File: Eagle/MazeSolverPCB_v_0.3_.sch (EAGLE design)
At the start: 26 parts, among them X1 TSW-113-02-S-S, X2 TSW-116-02-S-S, X3 TSW-113-02-S-S, X4 TSW-103-02-S-S, X5 TSW-103-02-S-S, X6 TSW-103-02-S-S, X7 TSW-103-02-S-S

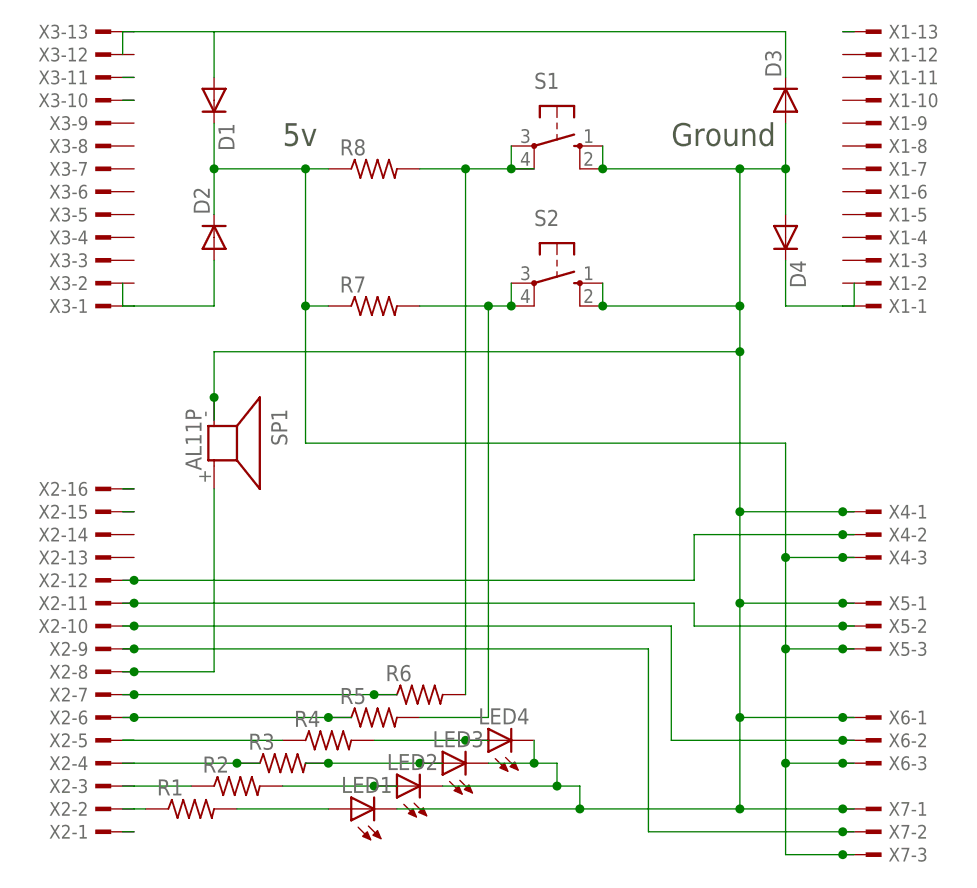
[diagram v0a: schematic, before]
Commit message: Fixed Eagle routing.
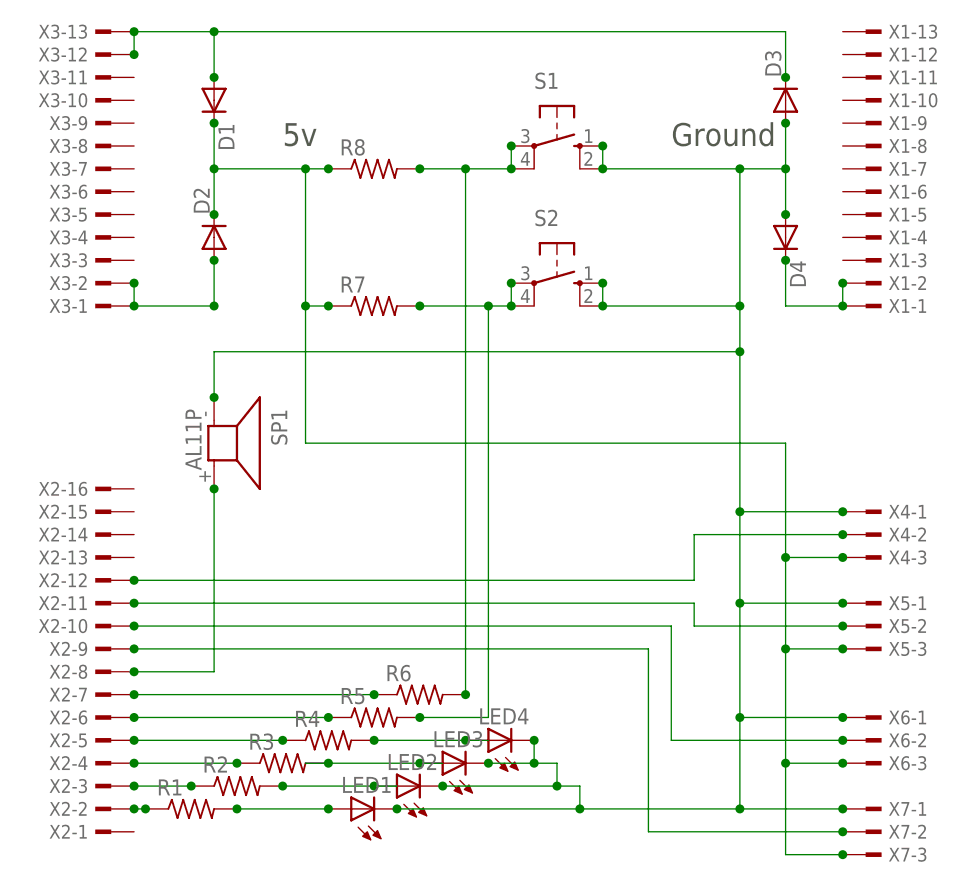
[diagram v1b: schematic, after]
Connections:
- removed net N$16: X2-16.1
- removed net N$18: X3-10.1
- removed net N$22: X1-13.1
- removed net N$23: X3-11.1
- removed net N$24: D2.A, X3-1.1
- removed net N$31: X2-15.1
- removed net N$6 (its old number): X2-1.1
- removed net N$9 (its old number): R4.1
- new net N$15: D2.A, X3-1.1, X3-2.1
- net N$20: now also X3-12.1
- net N$25: now also R4.1
- net N$8: now also X1-2.1
